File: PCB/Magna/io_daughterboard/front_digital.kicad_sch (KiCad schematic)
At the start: 73 parts, among them U1801 XL9535

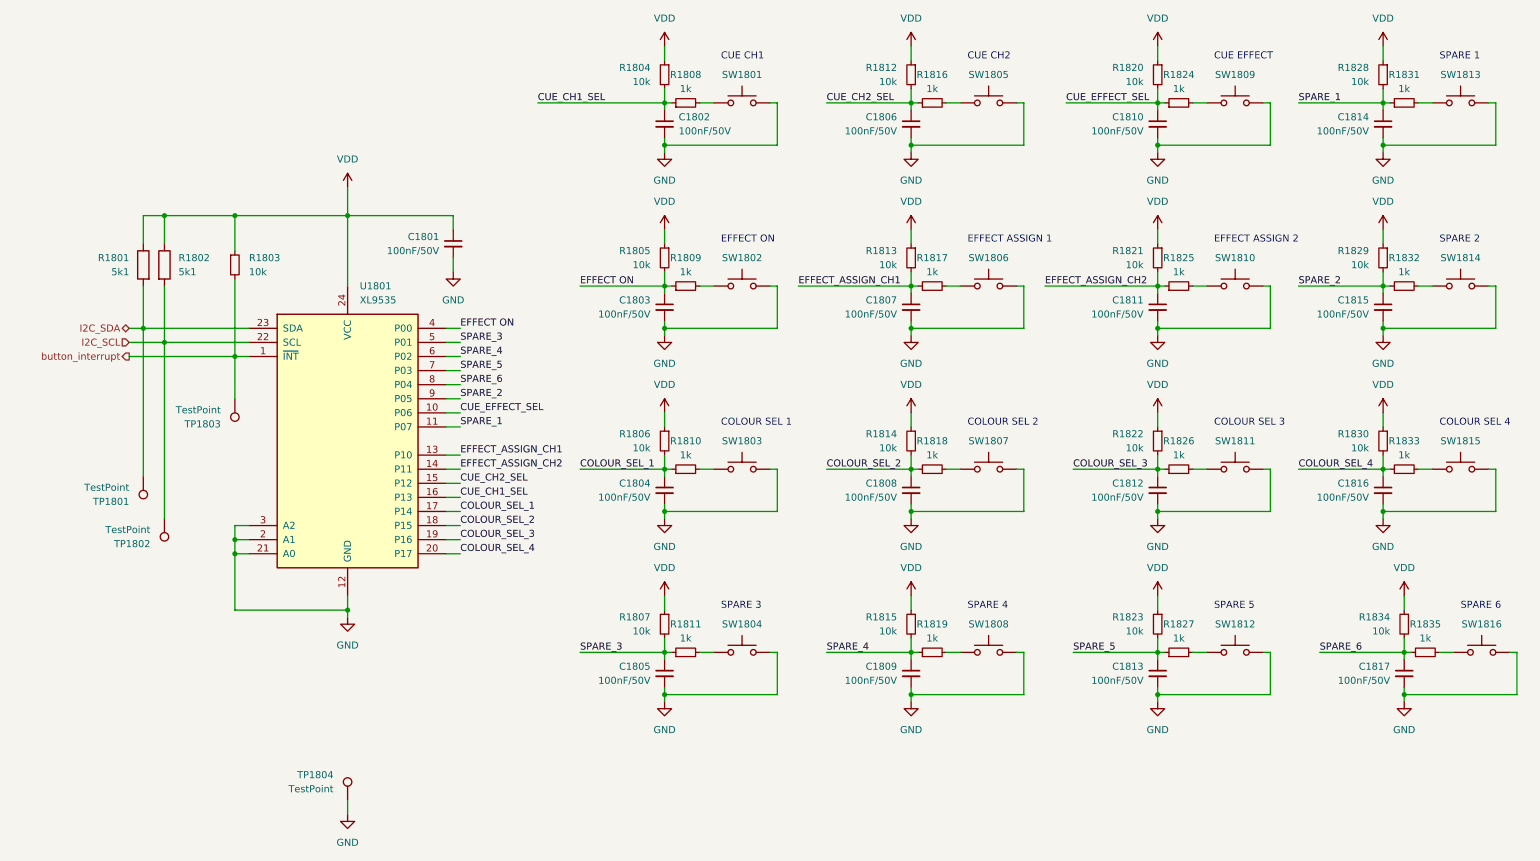
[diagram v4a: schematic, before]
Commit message: Change all capacitors to 22uF on IO board(#5)
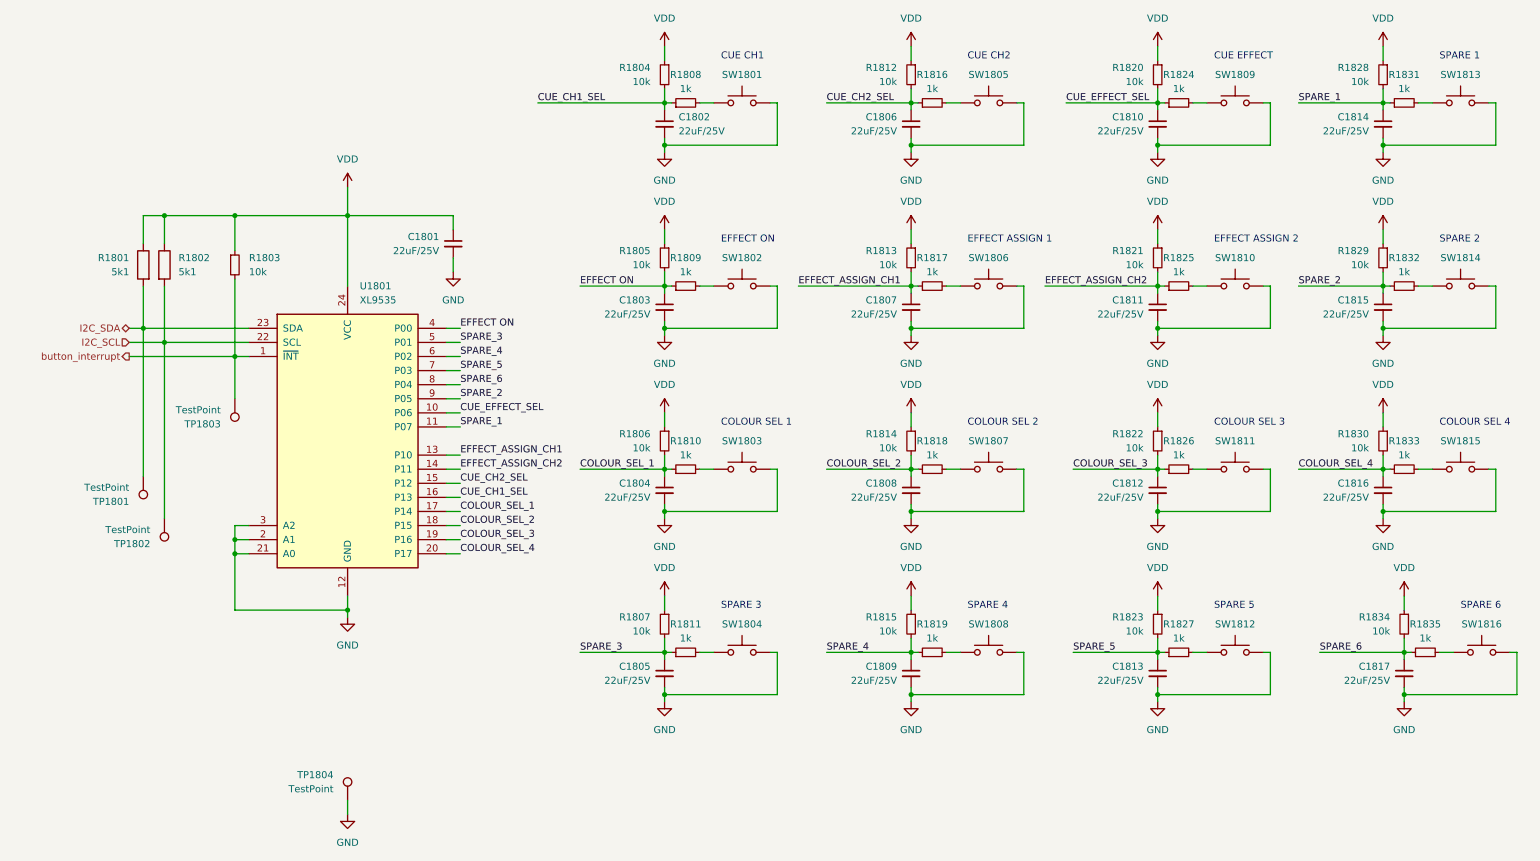
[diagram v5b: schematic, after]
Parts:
- C1801, C1802, C1803, C1804, C1805, C1806, C1807, C1808, C1809, C1810, C1811, C1812, C1813, C1814, C1815, C1816, C1817: value 100nF/50V -> 22uF/25V; LCSC C49678 -> C45783
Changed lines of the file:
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@@
       (effects (font (size 1.27 1.27)) (justify right))
     )
-    (property "Value" "100nF/50V" (at 251.46 144.7863 0)
+    (property "Value" "22uF/25V" (at 251.46 144.7863 0)
       (effects (font (size 1.27 1.27)) (justify right))
     )
@@
       (effects (font (size 1.27 1.27)) hide)
     )
-    (property "LCSC" "C49678" (at 254 143.51 0)
+    (property "LCSC" "C45783" (at 254 143.51 0)
       (effects (font (size 1.27 1.27)) hide)
     )
@@
       (effects (font (size 1.27 1.27)) (justify right))
     )
-    (property "Value" "100nF/50V" (at 247.65 45.7263 0)
+    (property "Value" "22uF/25V" (at 247.65 45.7263 0)
       (effects (font (size 1.27 1.27)) (justify right))
     )
@@
       (effects (font (size 1.27 1.27)) hide)
     )
-    (property "LCSC" "C49678" (at 250.19 44.45 0)
+    (property "LCSC" "C45783" (at 250.19 44.45 0)
       (effects (font (size 1.27 1.27)) hide)
     )
@@
       (effects (font (size 1.27 1.27)) (justify right))
     )
-    (property "Value" "100nF/50V" (at 207.01 111.7663 0)
+    (property "Value" "22uF/25V" (at 207.01 111.7663 0)
       (effects (font (size 1.27 1.27)) (justify right))
     )
@@
       (effects (font (size 1.27 1.27)) hide)
     )
-    (property "LCSC" "C49678" (at 209.55 110.49 0)
+    (property "LCSC" "C45783" (at 209.55 110.49 0)
       (effects (font (size 1.27 1.27)) hide)
     )
@@
       (effects (font (size 1.27 1.27)) (justify right))
     )
-    (property "Value" "100nF/50V" (at 207.01 144.7863 0)
+    (property "Value" "22uF/25V" (at 207.01 144.7863 0)
       (effects (font (size 1.27 1.27)) (justify right))
     )
@@
       (effects (font (size 1.27 1.27)) hide)
     )
-    (property "LCSC" "C49678" (at 209.55 143.51 0)
+    (property "LCSC" "C45783" (at 209.55 143.51 0)
       (effects (font (size 1.27 1.27)) hide)
     )
@@
       (effects (font (size 1.27 1.27)) (justify right))
     )
-    (property "Value" "100nF/50V" (at 207.01 78.7463 0)
+    (property "Value" "22uF/25V" (at 207.01 78.7463 0)
       (effects (font (size 1.27 1.27)) (justify right))
     )
@@
       (effects (font (size 1.27 1.27)) hide)
     )
-    (property "LCSC" "C49678" (at 209.55 77.47 0)
+    (property "LCSC" "C45783" (at 209.55 77.47 0)
       (effects (font (size 1.27 1.27)) hide)
     )
@@
       (effects (font (size 1.27 1.27)) (justify right))
     )
-    (property "Value" "100nF/50V" (at 118.11 78.7463 0)
+    (property "Value" "22uF/25V" (at 118.11 78.7463 0)
       (effects (font (size 1.27 1.27)) (justify right))
     )
@@
       (effects (font (size 1.27 1.27)) hide)
     )
-    (property "LCSC" "C49678" (at 120.65 77.47 0)
+    (property "LCSC" "C45783" (at 120.65 77.47 0)
       (effects (font (size 1.27 1.27)) hide)
     )
@@
       (effects (font (size 1.27 1.27)) (justify right))
     )
-    (property "Value" "100nF/50V" (at 118.11 111.7663 0)
+    (property "Value" "22uF/25V" (at 118.11 111.7663 0)
       (effects (font (size 1.27 1.27)) (justify right))
     )
@@
       (effects (font (size 1.27 1.27)) hide)
     )
-    (property "LCSC" "C49678" (at 120.65 110.49 0)
+    (property "LCSC" "C45783" (at 120.65 110.49 0)
       (effects (font (size 1.27 1.27)) hide)
     )
@@
       (effects (font (size 1.27 1.27)) (justify right))
     )
-    (property "Value" "100nF/50V" (at 80.01 67.3163 0)
+    (property "Value" "22uF/25V" (at 80.01 67.3163 0)
       (effects (font (size 1.27 1.27)) (justify right))
     )
@@
       (effects (font (size 1.27 1.27)) hide)
     )
-    (property "LCSC" "C49678" (at 82.55 66.04 0)
+    (property "LCSC" "C45783" (at 82.55 66.04 0)
       (effects (font (size 1.27 1.27)) hide)
     )
@@
       (effects (font (size 1.27 1.27)) (justify right))
     )
-    (property "Value" "100nF/50V" (at 162.56 144.7863 0)
+    (property "Value" "22uF/25V" (at 162.56 144.7863 0)
       (effects (font (size 1.27 1.27)) (justify right))
     )
@@
       (effects (font (size 1.27 1.27)) hide)
     )
-    (property "LCSC" "C49678" (at 165.1 143.51 0)
+    (property "LCSC" "C45783" (at 165.1 143.51 0)
       (effects (font (size 1.27 1.27)) hide)
     )
@@
       (effects (font (size 1.27 1.27)) (justify right))
     )
-    (property "Value" "100nF/50V" (at 162.56 111.7663 0)
+    (property "Value" "22uF/25V" (at 162.56 111.7663 0)
       (effects (font (size 1.27 1.27)) (justify right))
     )
@@
       (effects (font (size 1.27 1.27)) hide)
     )
-    (property "LCSC" "C49678" (at 165.1 110.49 0)
+    (property "LCSC" "C45783" (at 165.1 110.49 0)
       (effects (font (size 1.27 1.27)) hide)
     )
@@
       (effects (font (size 1.27 1.27)) (justify right))
     )
-    (property "Value" "100nF/50V" (at 207.01 45.7263 0)
+    (property "Value" "22uF/25V" (at 207.01 45.7263 0)
       (effects (font (size 1.27 1.27)) (justify right))
     )
@@
       (effects (font (size 1.27 1.27)) hide)
     )
-    (property "LCSC" "C49678" (at 209.55 44.45 0)
+    (property "LCSC" "C45783" (at 209.55 44.45 0)
       (effects (font (size 1.27 1.27)) hide)
     )
@@
       (effects (font (size 1.27 1.27)) (justify right))
     )
-    (property "Value" "100nF/50V" (at 247.65 111.7663 0)
+    (property "Value" "22uF/25V" (at 247.65 111.7663 0)
       (effects (font (size 1.27 1.27)) (justify right))
     )
@@
       (effects (font (size 1.27 1.27)) hide)
     )
-    (property "LCSC" "C49678" (at 250.19 110.49 0)
+    (property "LCSC" "C45783" (at 250.19 110.49 0)
       (effects (font (size 1.27 1.27)) hide)
     )
@@
       (effects (font (size 1.27 1.27)) (justify right))
     )
-    (property "Value" "100nF/50V" (at 162.56 78.7463 0)
+    (property "Value" "22uF/25V" (at 162.56 78.7463 0)
       (effects (font (size 1.27 1.27)) (justify right))
     )
@@
       (effects (font (size 1.27 1.27)) hide)
     )
-    (property "LCSC" "C49678" (at 165.1 77.47 0)
+    (property "LCSC" "C45783" (at 165.1 77.47 0)
       (effects (font (size 1.27 1.27)) hide)
     )
@@
       (effects (font (size 1.27 1.27)) (justify right))
     )
-    (property "Value" "100nF/50V" (at 162.56 45.7263 0)
+    (property "Value" "22uF/25V" (at 162.56 45.7263 0)
       (effects (font (size 1.27 1.27)) (justify right))
     )
@@
       (effects (font (size 1.27 1.27)) hide)
     )
-    (property "LCSC" "C49678" (at 165.1 44.45 0)
+    (property "LCSC" "C45783" (at 165.1 44.45 0)
       (effects (font (size 1.27 1.27)) hide)
     )
@@
       (effects (font (size 1.27 1.27)) (justify right))
     )
-    (property "Value" "100nF/50V" (at 123.19 45.7263 0)
+    (property "Value" "22uF/25V" (at 123.19 45.7263 0)
       (effects (font (size 1.27 1.27)) (justify right))
     )
@@
       (effects (font (size 1.27 1.27)) hide)
     )
-    (property "LCSC" "C49678" (at 120.65 44.45 0)
+    (property "LCSC" "C45783" (at 120.65 44.45 0)
       (effects (font (size 1.27 1.27)) hide)
     )
@@
       (effects (font (size 1.27 1.27)) (justify right))
     )
-    (property "Value" "100nF/50V" (at 118.11 144.7863 0)
+    (property "Value" "22uF/25V" (at 118.11 144.7863 0)
       (effects (font (size 1.27 1.27)) (justify right))
     )
@@
       (effects (font (size 1.27 1.27)) hide)
     )
-    (property "LCSC" "C49678" (at 120.65 143.51 0)
+    (property "LCSC" "C45783" (at 120.65 143.51 0)
       (effects (font (size 1.27 1.27)) hide)
     )
@@
       (effects (font (size 1.27 1.27)) (justify right))
     )
-    (property "Value" "100nF/50V" (at 247.65 78.7463 0)
+    (property "Value" "22uF/25V" (at 247.65 78.7463 0)
       (effects (font (size 1.27 1.27)) (justify right))
     )
@@
       (effects (font (size 1.27 1.27)) hide)
     )
-    (property "LCSC" "C49678" (at 250.19 77.47 0)
+    (property "LCSC" "C45783" (at 250.19 77.47 0)
       (effects (font (size 1.27 1.27)) hide)
     )

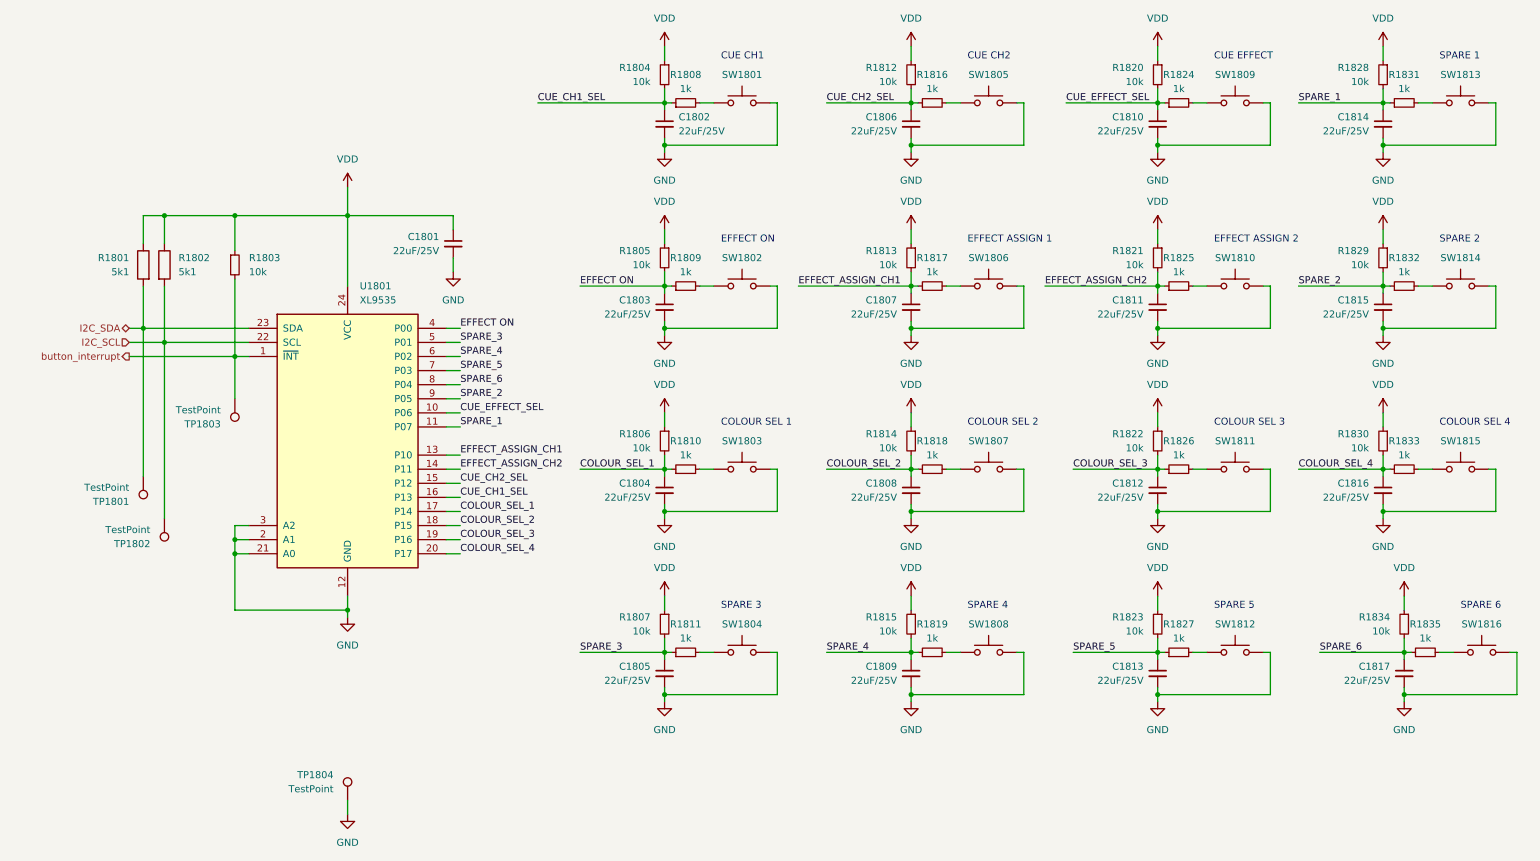
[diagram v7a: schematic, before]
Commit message: Update schematics to Kicad 9
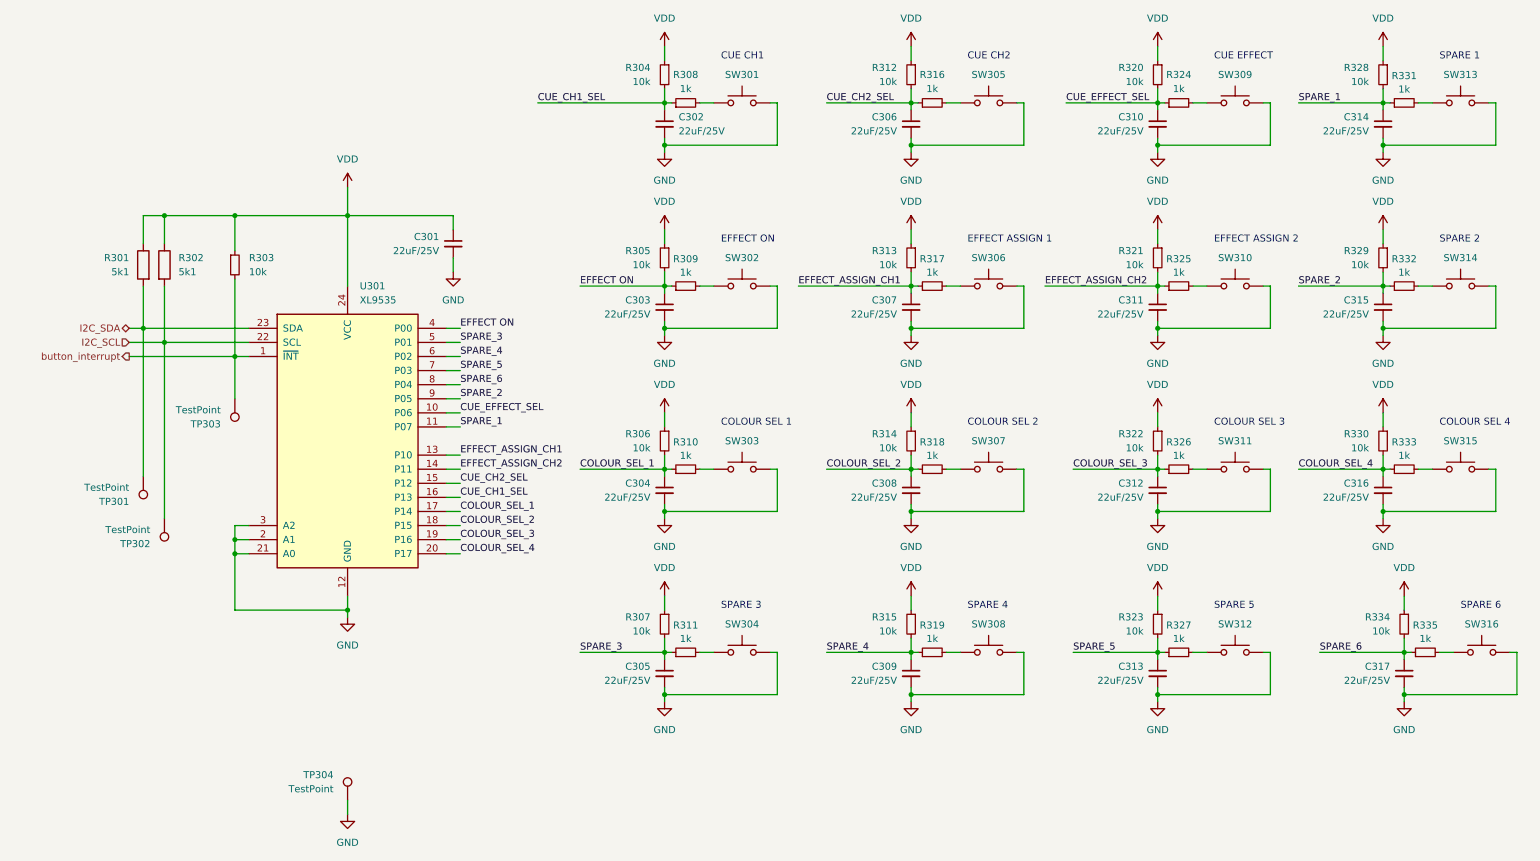
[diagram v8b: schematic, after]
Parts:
- renumbered C1801 to C301, C1802 to C302, C1803 to C303, C1804 to C304, C1805 to C305, C1806 to C306, C1807 to C307, C1808 to C308, C1809 to C309, C1810 to C310, C1811 to C311, C1812 to C312, C1813 to C313, C1814 to C314, C1815 to C315, C1816 to C316, C1817 to C317, R1801 to R301, R1802 to R302, R1803 to R303, R1804 to R304, R1805 to R305, R1806 to R306, R1807 to R307, R1808 to R308, R1809 to R309, R1810 to R310, R1811 to R311, R1812 to R312, R1813 to R313, R1814 to R314, R1815 to R315, R1816 to R316, R1817 to R317, R1818 to R318, R1819 to R319, R1820 to R320, R1821 to R321, R1822 to R322, R1823 to R323, R1824 to R324, R1825 to R325, R1826 to R326, R1827 to R327, R1828 to R328, R1829 to R329, R1830 to R330, R1831 to R331, R1832 to R332, R1833 to R333, R1834 to R334, R1835 to R335, SW1801 to SW301, SW1802 to SW302, SW1803 to SW303, SW1804 to SW304, SW1805 to SW305, SW1806 to SW306, SW1807 to SW307, SW1808 to SW308, SW1809 to SW309, SW1810 to SW310, SW1811 to SW311, SW1812 to SW312, SW1813 to SW313, SW1814 to SW314, SW1815 to SW315, SW1816 to SW316, TP1801 to TP301, TP1802 to TP302, TP1803 to TP303, TP1804 to TP304, U1801 to U301
